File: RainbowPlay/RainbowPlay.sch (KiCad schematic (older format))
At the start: 72 parts, among them J1 GPIO_CONNECTOR, J2 Conn_01x08_Male, J3 Conn_01x04_Male, J4 Conn_01x02_Male, J5 Conn_01x02_Male, Q1 BSS138, Q2 BSS138, Q3 BSS138, Q4 BSS138, Q5 BSS138, U1 TPA2001D2, U2 SN74LVC1G32DBVRG4

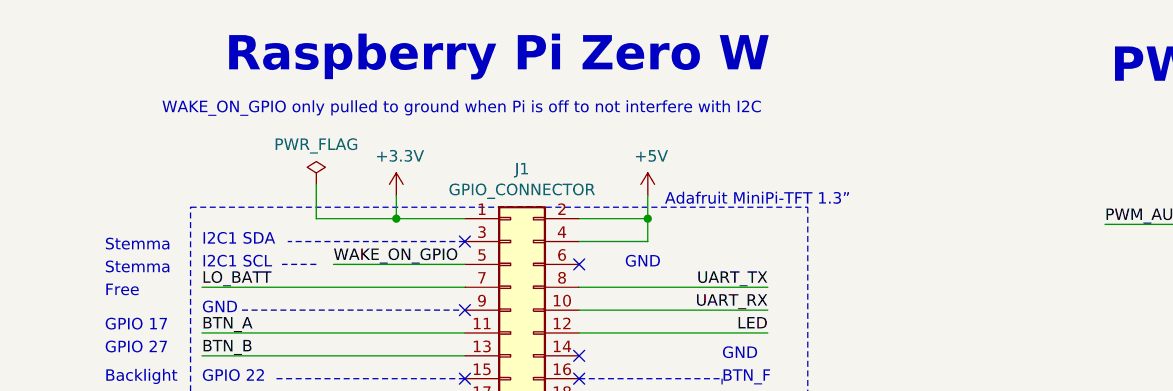
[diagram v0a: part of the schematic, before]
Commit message: Add pico
- Add pico
- Add example neopixel code
- Test neopixel with pico (works)
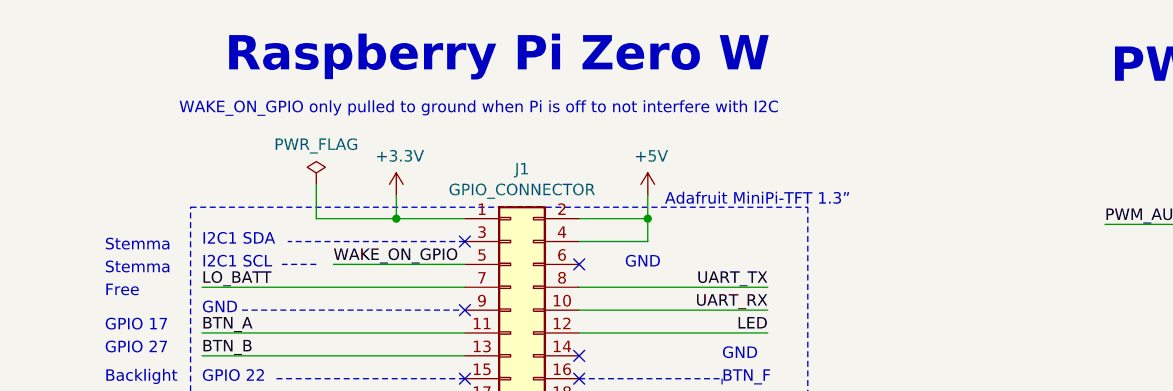
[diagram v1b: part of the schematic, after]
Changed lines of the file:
@@
 Text Notes 500  1925 0    50   ~ 0
 Stemma
-Text Notes 750  1325 0    50   ~ 0
+Text Notes 825  1325 0    50   ~ 0
 WAKE_ON_GPIO only pulled to ground when Pi is off to not interfere with I2C
 Text Notes 500  2825 0    50   ~ 0
